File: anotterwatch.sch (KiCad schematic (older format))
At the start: 55 parts, among them J1 USB_C_Receptacle_USB2.0, J3 Micro_SD_Card, Q1 AO3400, Q3 npn, Q4 npn, U1 TP4056, U12 BMI270, U2 ESP32, U3 CH340C, U4 ST7789V

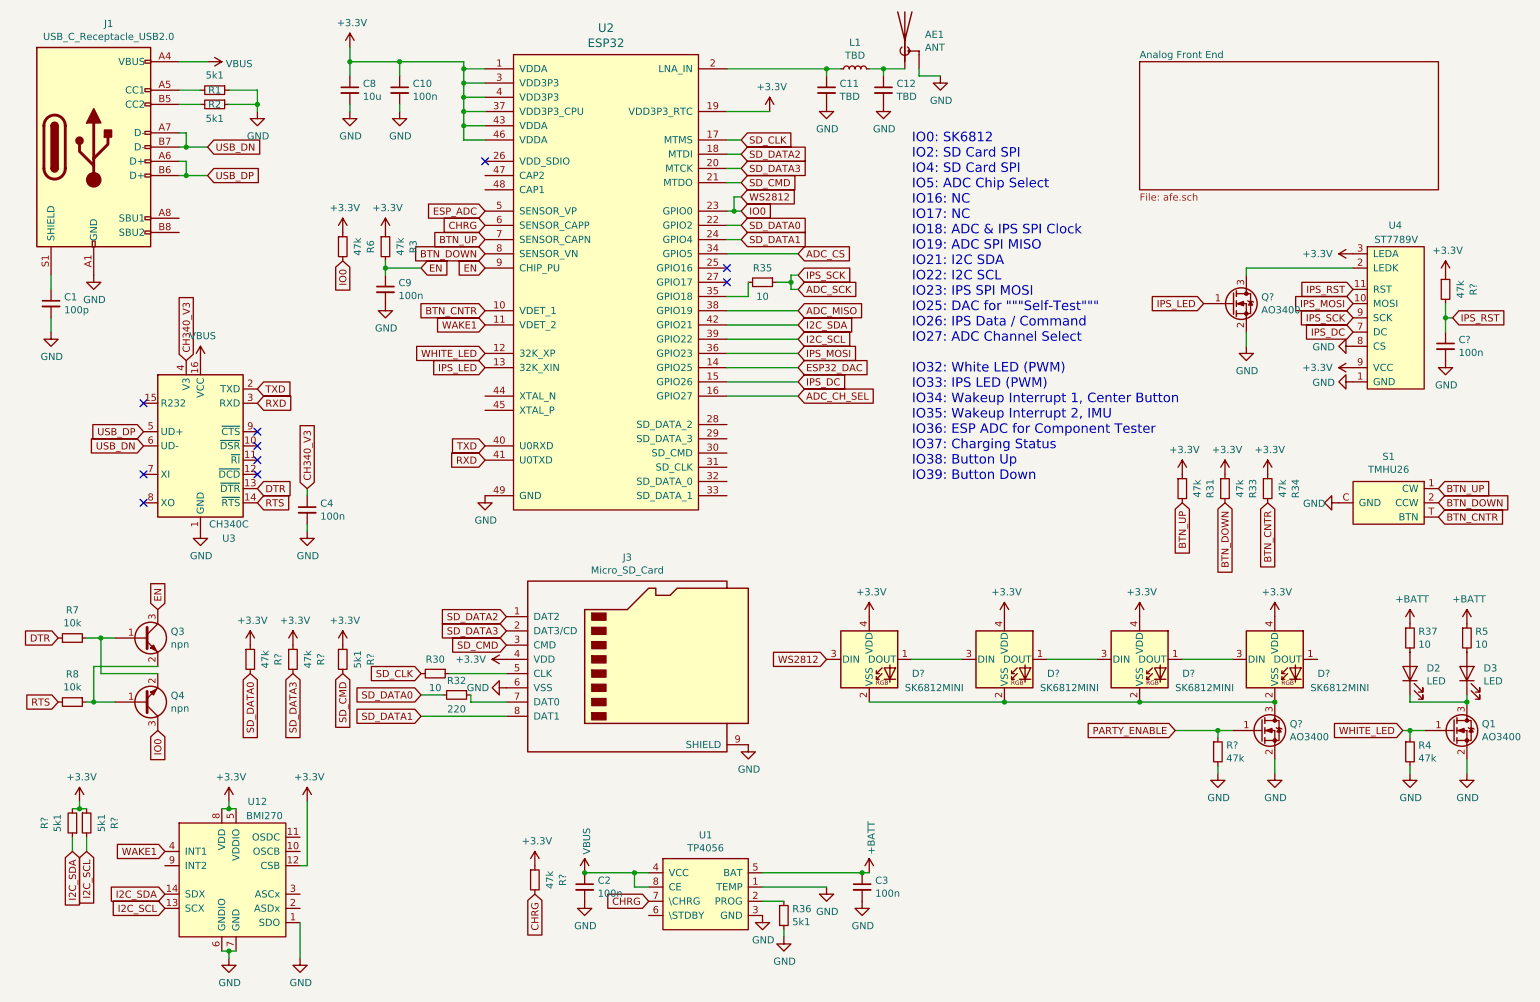
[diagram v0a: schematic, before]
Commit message: ADD: speaker
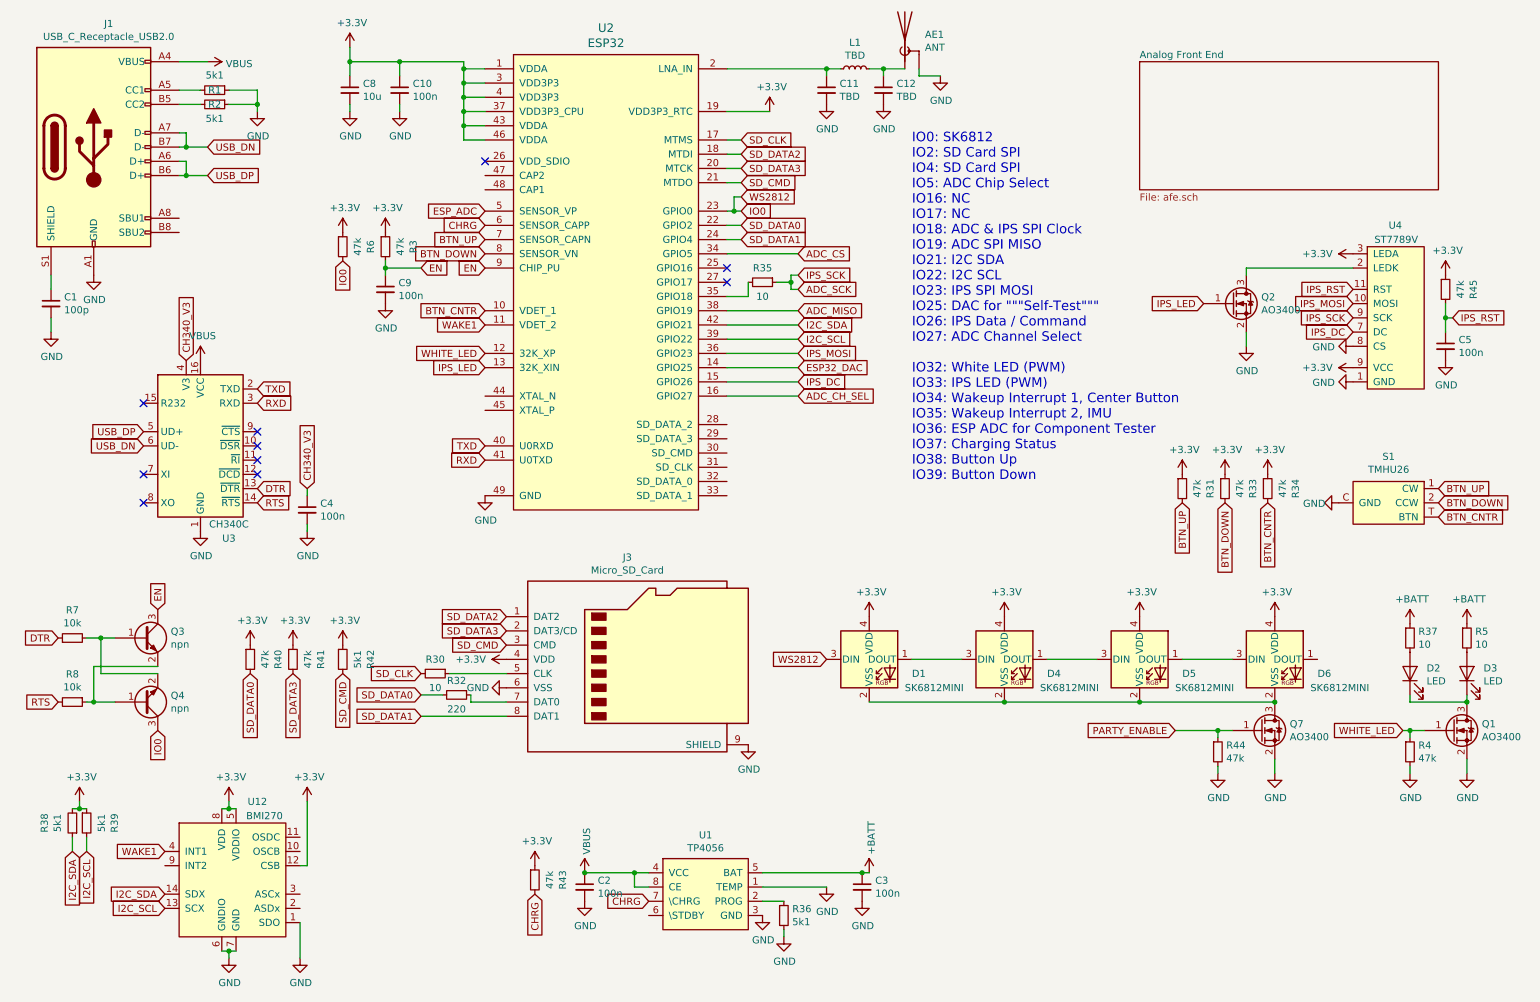
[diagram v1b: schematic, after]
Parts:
- gave numbers to parts that had none: 15
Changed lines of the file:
@@
 	9300 3100 9300 3200
 $Comp
-L power:+3.3V #PWR?
+L power:+3.3V #PWR057
 U 1 1 5C88B593
 P 10050 3350
-F 0 "#PWR?" H 10050 3200 50  0001 C CNN
+F 0 "#PWR057" H 10050 3200 50  0001 C CNN
 F 1 "+3.3V" V 10050 3600 50  0000 C CNN
 F 2 "" H 10050 3350 50  0001 C CNN
@@
 CHRG
 $Comp
-L Device:R_Small R?
+L Device:R_Small R43
 U 1 1 5C8A8B52
 P 4300 6950
-F 0 "R?" V 4496 6950 50  0000 C CNN
+F 0 "R43" V 4496 6950 50  0000 C CNN
 F 1 "47k" V 4405 6950 50  0000 C CNN
 F 2 "Resistor_SMD:R_0603_1608Metric" H 4300 6950 50  0001 C CNN
@@
 $EndComp
 $Comp
-L power:+3.3V #PWR?
+L power:+3.3V #PWR049
 U 1 1 5C8A8B59
 P 4300 6850
-F 0 "#PWR?" H 4300 6700 50  0001 C CNN
+F 0 "#PWR049" H 4300 6700 50  0001 C CNN
 F 1 "+3.3V" H 4315 7023 50  0000 C CNN
 F 2 "" H 4300 6850 50  0001 C CNN
@@
 $EndComp
 $Comp
-L Device:Q_NMOS_GSD Q?
+L Device:Q_NMOS_GSD Q2
 U 1 1 5C8ADB53
 P 9200 2900
-F 0 "Q?" H 9405 2946 50  0000 L CNN
+F 0 "Q2" H 9405 2946 50  0000 L CNN
 F 1 "AO3400" H 9405 2855 50  0000 L CNN
 F 2 "Package_TO_SOT_SMD:SOT-23" H 9400 3000 50  0001 C CNN
@@
 IPS_MOSI
 $Comp
-L power:+3.3V #PWR?
+L power:+3.3V #PWR03
 U 1 1 5C8AE78F
 P 2150 6400
-F 0 "#PWR?" H 2150 6250 50  0001 C CNN
+F 0 "#PWR03" H 2150 6250 50  0001 C CNN
 F 1 "+3.3V" H 2165 6573 50  0000 C CNN
 F 2 "" H 2150 6400 50  0001 C CNN
@@
 Connection ~ 2150 6450
 $Comp
-L power:GND #PWR?
+L power:GND #PWR06
 U 1 1 5C8B6736
 P 2150 7500
-F 0 "#PWR?" H 2150 7250 50  0001 C CNN
+F 0 "#PWR06" H 2150 7250 50  0001 C CNN
 F 1 "GND" H 2155 7327 50  0000 C CNN
 F 2 "" H 2150 7500 50  0001 C CNN
@@
 Connection ~ 2150 7450
 $Comp
-L power:GND #PWR?
+L power:GND #PWR046
 U 1 1 5C8C0040
 P 2650 7500
-F 0 "#PWR?" H 2650 7250 50  0001 C CNN
+F 0 "#PWR046" H 2650 7250 50  0001 C CNN
 F 1 "GND" H 2655 7327 50  0000 C CNN
 F 2 "" H 2650 7500 50  0001 C CNN
@@
 I2C_SCL
 $Comp
-L power:+3.3V #PWR?
+L power:+3.3V #PWR047
 U 1 1 5C8CE265
 P 2700 6400
-F 0 "#PWR?" H 2700 6250 50  0001 C CNN
+F 0 "#PWR047" H 2700 6250 50  0001 C CNN
 F 1 "+3.3V" H 2715 6573 50  0000 C CNN
 F 2 "" H 2700 6400 50  0001 C CNN
@@
 I2C_SCL
 $Comp
-L power:+3.3V #PWR?
+L power:+3.3V #PWR01
 U 1 1 5C8EA6C1
 P 1100 6400
-F 0 "#PWR?" H 1100 6250 50  0001 C CNN
+F 0 "#PWR01" H 1100 6250 50  0001 C CNN
 F 1 "+3.3V" H 1115 6573 50  0000 C CNN
 F 2 "" H 1100 6400 50  0001 C CNN
@@
 $EndComp
 $Comp
-L Device:R_Small R?
+L Device:R_Small R39
 U 1 1 5C8EA748
 P 1150 6550
-F 0 "R?" V 1346 6550 50  0000 C CNN
+F 0 "R39" V 1346 6550 50  0000 C CNN
 F 1 "5k1" V 1255 6550 50  0000 C CNN
 F 2 "Resistor_SMD:R_0603_1608Metric" H 1150 6550 50  0001 C CNN
@@
 $EndComp
 $Comp
-L Device:R_Small R?
+L Device:R_Small R38
 U 1 1 5C8EA7F2
 P 1050 6550
-F 0 "R?" V 1246 6550 50  0000 C CNN
+F 0 "R38" V 1246 6550 50  0000 C CNN
 F 1 "5k1" V 1155 6550 50  0000 C CNN
 F 2 "Resistor_SMD:R_0603_1608Metric" H 1050 6550 50  0001 C CNN
@@
 SD_CMD
 $Comp
-L Device:R_Small R?
+L Device:R_Small R40
 U 1 1 5CA0E021
 P 2300 5400
-F 0 "R?" V 2496 5400 50  0000 C CNN
+F 0 "R40" V 2496 5400 50  0000 C CNN
 F 1 "47k" V 2405 5400 50  0000 C CNN
 F 2 "Resistor_SMD:R_0603_1608Metric" H 2300 5400 50  0001 C CNN
@@
 $EndComp
 $Comp
-L Device:R_Small R?
+L Device:R_Small R41
 U 1 1 5CA0E103
 P 2600 5400
-F 0 "R?" V 2796 5400 50  0000 C CNN
+F 0 "R41" V 2796 5400 50  0000 C CNN
 F 1 "47k" V 2705 5400 50  0000 C CNN
 F 2 "Resistor_SMD:R_0603_1608Metric" H 2600 5400 50  0001 C CNN
@@
 $EndComp
 $Comp
-L power:+3.3V #PWR?
+L power:+3.3V #PWR039
 U 1 1 5CA0E26B
 P 2300 5300
-F 0 "#PWR?" H 2300 5150 50  0001 C CNN
+F 0 "#PWR039" H 2300 5150 50  0001 C CNN
 F 1 "+3.3V" H 2315 5473 50  0000 C CNN
 F 2 "" H 2300 5300 50  0001 C CNN
@@
 $EndComp
 $Comp
-L power:+3.3V #PWR?
+L power:+3.3V #PWR040
 U 1 1 5CA0E2FA
 P 2600 5300
-F 0 "#PWR?" H 2600 5150 50  0001 C CNN
+F 0 "#PWR040" H 2600 5150 50  0001 C CNN
 F 1 "+3.3V" H 2615 5473 50  0000 C CNN
 F 2 "" H 2600 5300 50  0001 C CNN
@@
 $EndComp
 $Comp
-L Device:R_Small R?
+L Device:R_Small R42
 U 1 1 5CA0E451
 P 2950 5400
-F 0 "R?" V 3146 5400 50  0000 C CNN
+F 0 "R42" V 3146 5400 50  0000 C CNN
 F 1 "5k1" V 3055 5400 50  0000 C CNN
 F 2 "Resistor_SMD:R_0603_1608Metric" H 2950 5400 50  0001 C CNN
@@
 $EndComp
 $Comp
-L power:+3.3V #PWR?
+L power:+3.3V #PWR048
 U 1 1 5CA0E551
 P 2950 5300
-F 0 "#PWR?" H 2950 5150 50  0001 C CNN
+F 0 "#PWR048" H 2950 5150 50  0001 C CNN
 F 1 "+3.3V" H 2965 5473 50  0000 C CNN
 F 2 "" H 2950 5300 50  0001 C CNN
@@
 SD_DATA1
 $Comp
-L LED:SK6812MINI D?
+L LED:SK6812MINI D1
 U 1 1 5CA5E3A4
 P 6650 5400
-F 0 "D?" H 6950 5300 50  0000 L CNN
+F 0 "D1" H 6950 5300 50  0000 L CNN
 F 1 "SK6812MINI" H 6900 5200 50  0000 L CNN
 F 2 "LED_SMD:LED_SK6812MINI_PLCC4_3.5x3.5mm_P1.75mm" H 6700 5100 50  0001 L TNN
@@
 $EndComp
 $Comp
-L LED:SK6812MINI D?
+L LED:SK6812MINI D4
 U 1 1 5CA5E80C
 P 7600 5400
-F 0 "D?" H 7900 5300 50  0000 L CNN
+F 0 "D4" H 7900 5300 50  0000 L CNN
 F 1 "SK6812MINI" H 7850 5200 50  0000 L CNN
 F 2 "LED_SMD:LED_SK6812MINI_PLCC4_3.5x3.5mm_P1.75mm" H 7650 5100 50  0001 L TNN
@@
 $EndComp
 $Comp
-L LED:SK6812MINI D?
+L LED:SK6812MINI D5
 U 1 1 5CA5E8A0
 P 8550 5400
-F 0 "D?" H 8850 5300 50  0000 L CNN
+F 0 "D5" H 8850 5300 50  0000 L CNN
 F 1 "SK6812MINI" H 8800 5200 50  0000 L CNN
 F 2 "LED_SMD:LED_SK6812MINI_PLCC4_3.5x3.5mm_P1.75mm" H 8600 5100 50  0001 L TNN
@@
 $EndComp
 $Comp
-L LED:SK6812MINI D?
+L LED:SK6812MINI D6
 U 1 1 5CA5E934
 P 9500 5400
-F 0 "D?" H 9800 5300 50  0000 L CNN
+F 0 "D6" H 9800 5300 50  0000 L CNN
 F 1 "SK6812MINI" H 9750 5200 50  0000 L CNN
 F 2 "LED_SMD:LED_SK6812MINI_PLCC4_3.5x3.5mm_P1.75mm" H 9550 5100 50  0001 L TNN
@@
 	8850 5400 9200 5400
 $Comp
-L power:+3.3V #PWR?
+L power:+3.3V #PWR050
 U 1 1 5CA6F675
 P 6650 5100
-F 0 "#PWR?" H 6650 4950 50  0001 C CNN
+F 0 "#PWR050" H 6650 4950 50  0001 C CNN
 F 1 "+3.3V" H 6665 5273 50  0000 C CNN
 F 2 "" H 6650 5100 50  0001 C CNN
@@
 $EndComp
 $Comp
-L power:+3.3V #PWR?
+L power:+3.3V #PWR051
 U 1 1 5CA6F6ED
 P 7600 5100
-F 0 "#PWR?" H 7600 4950 50  0001 C CNN
+F 0 "#PWR051" H 7600 4950 50  0001 C CNN
 F 1 "+3.3V" H 7615 5273 50  0000 C CNN
 F 2 "" H 7600 5100 50  0001 C CNN
@@
 $EndComp
 $Comp
-L power:+3.3V #PWR?
+L power:+3.3V #PWR052
 U 1 1 5CA6F75E
 P 8550 5100
-F 0 "#PWR?" H 8550 4950 50  0001 C CNN
+F 0 "#PWR052" H 8550 4950 50  0001 C CNN
 F 1 "+3.3V" H 8565 5273 50  0000 C CNN
 F 2 "" H 8550 5100 50  0001 C CNN
@@
 $EndComp
 $Comp
-L power:+3.3V #PWR?
+L power:+3.3V #PWR054
 U 1 1 5CA6F7CF
 P 9500 5100
-F 0 "#PWR?" H 9500 4950 50  0001 C CNN
+F 0 "#PWR054" H 9500 4950 50  0001 C CNN
 F 1 "+3.3V" H 9515 5273 50  0000 C CNN
 F 2 "" H 9500 5100 50  0001 C CNN
@@
 $EndComp
 $Comp
-L Device:Q_NMOS_GSD Q?
+L Device:Q_NMOS_GSD Q7
 U 1 1 5CA73CF2
 P 9400 5900
-F 0 "Q?" H 9605 5946 50  0000 L CNN
+F 0 "Q7" H 9605 5946 50  0000 L CNN
 F 1 "AO3400" H 9605 5855 50  0000 L CNN
 F 2 "Package_TO_SOT_SMD:SOT-23" H 9600 6000 50  0001 C CNN
@@
 $EndComp
 $Comp
-L power:GND #PWR?
+L power:GND #PWR055
 U 1 1 5CA73CF9
 P 9500 6200
-F 0 "#PWR?" H 9500 5950 50  0001 C CNN
+F 0 "#PWR055" H 9500 5950 50  0001 C CNN
 F 1 "GND" H 9505 6027 50  0000 C CNN
 F 2 "" H 9500 6200 50  0001 C CNN
@@
 	9500 6200 9500 6100
 $Comp
-L Device:R_Small R?
+L Device:R_Small R44
 U 1 1 5CA73D00
 P 9100 6050
-F 0 "R?" H 9159 6096 50  0000 L CNN
+F 0 "R44" H 9159 6096 50  0000 L CNN
 F 1 "47k" H 9159 6005 50  0000 L CNN
 F 2 "Resistor_SMD:R_0603_1608Metric" H 9100 6050 50  0001 C CNN
@@
 	9100 5900 9200 5900
 $Comp
-L power:GND #PWR?
+L power:GND #PWR053
 U 1 1 5CA73D0A
 P 9100 6200
-F 0 "#PWR?" H 9100 5950 50  0001 C CNN
+F 0 "#PWR053" H 9100 5950 50  0001 C CNN
 F 1 "GND" H 9105 6027 50  0000 C CNN
 F 2 "" H 9100 6200 50  0001 C CNN
@@
 Connection ~ 10450 5900
 $Comp
-L power:GND #PWR?
+L power:GND #PWR056
 U 1 1 5CB2DE24
 P 10050 3200
-F 0 "#PWR?" H 10050 2950 50  0001 C CNN
+F 0 "#PWR056" H 10050 2950 50  0001 C CNN
 F 1 "GND" V 10055 3072 50  0000 R CNN
 F 2 "" H 10050 3200 50  0001 C CNN
@@
 IPS_RST
 $Comp
-L Device:R_Small R?
+L Device:R_Small R45
 U 1 1 5CB2EA91
 P 10700 2800
-F 0 "R?" V 10896 2800 50  0000 C CNN
+F 0 "R45" V 10896 2800 50  0000 C CNN
 F 1 "47k" V 10805 2800 50  0000 C CNN
 F 2 "Resistor_SMD:R_0603_1608Metric" H 10700 2800 50  0001 C CNN
@@
 $EndComp
 $Comp
-L power:+3.3V #PWR?
+L power:+3.3V #PWR058
 U 1 1 5CB2EA98
 P 10700 2700
-F 0 "#PWR?" H 10700 2550 50  0001 C CNN
+F 0 "#PWR058" H 10700 2550 50  0001 C CNN
 F 1 "+3.3V" H 10715 2873 50  0000 C CNN
 F 2 "" H 10700 2700 50  0001 C CNN
@@
 $EndComp
 $Comp
-L Device:C_Small C?
+L Device:C_Small C5
 U 1 1 5CB333E1
 P 10700 3200
-F 0 "C?" H 10792 3246 50  0000 L CNN
+F 0 "C5" H 10792 3246 50  0000 L CNN
 F 1 "100n" H 10792 3155 50  0000 L CNN
 F 2 "Capacitor_SMD:C_0603_1608Metric" H 10700 3200 50  0001 C CNN
@@
 $EndComp
 $Comp
-L power:GND #PWR?
+L power:GND #PWR059
 U 1 1 5CB333E8
 P 10700 3300
-F 0 "#PWR?" H 10700 3050 50  0001 C CNN
+F 0 "#PWR059" H 10700 3050 50  0001 C CNN
 F 1 "GND" H 10705 3127 50  0000 C CNN
 F 2 "" H 10700 3300 50  0001 C CNN

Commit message: added power schematics
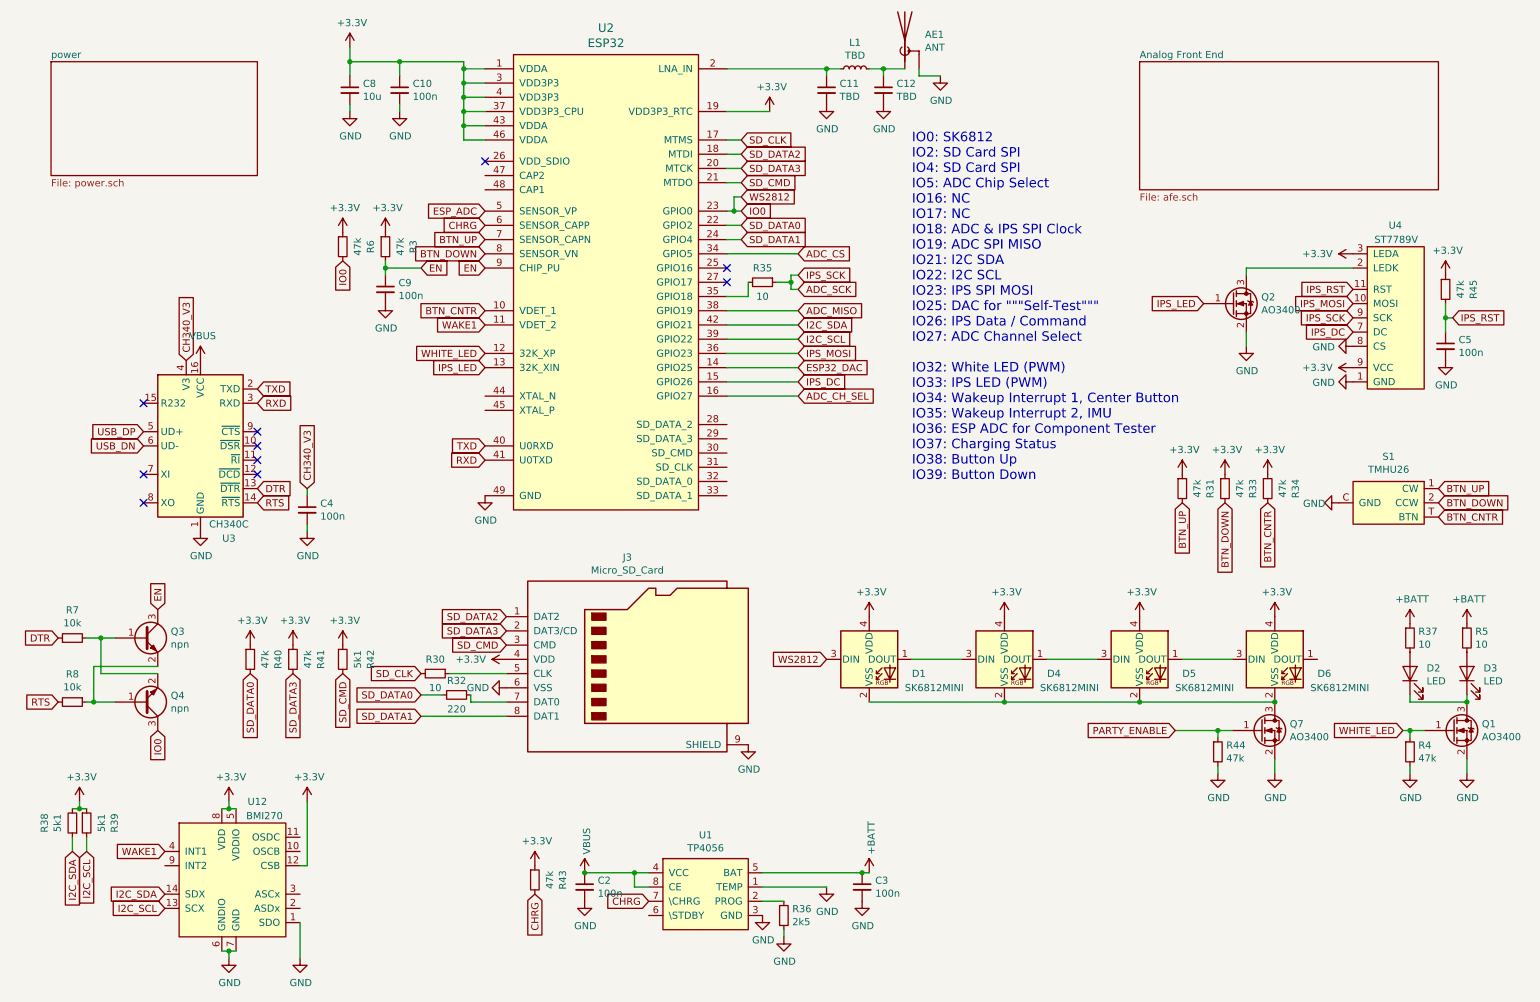
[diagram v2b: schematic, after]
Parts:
- removed C1: 100p, Capacitor_SMD:C_0603_1608Metric, symbol Device:C_Small
- removed J1: USB_C_Receptacle_USB2.0, badgelib:USB-C 16Pin, symbol anotterwatch-rescue:USB_C_Receptacle_USB2.0-Connector
- removed R1, R2: 5k1, Resistor_SMD:R_0603_1608Metric, symbol Device:R_Small
- R36: value 5k1 -> 2k5
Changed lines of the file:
@@
 $Descr A4 11693 8268
 encoding utf-8
-Sheet 1 2
+Sheet 1 3
 Title ""
 Date ""
@@
 Comment4 ""
 $EndDescr
-$Comp
-L anotterwatch-rescue:USB_C_Receptacle_USB2.0-Connector J1
-U 1 1 5C6DC086
-P 1200 1800
-F 0 "J1" H 1305 2667 50  0000 C CNN
-F 1 "USB_C_Receptacle_USB2.0" H 1305 2576 50  0000 C CNN
-F 2 "badgelib:USB-C 16Pin" H 1350 1800 50  0001 C CNN
-F 3 "https://nl.aliexpress.com/item/100PCS-LOT-USB-connector-Type-C-3-1-Female-connector-16Pin-SMD-SMT-Type-with-4/32822609480.html" H 1350 1800 50  0001 C CNN
-	1    1200 1800
-	1    0    0    -1
-$EndComp
-$Comp
-L power:GND #PWR0101
-U 1 1 5C6E198C
-P 1200 2700
-F 0 "#PWR0101" H 1200 2450 50  0001 C CNN
-F 1 "GND" H 1205 2527 50  0000 C CNN
-F 2 "" H 1200 2700 50  0001 C CNN
-F 3 "" H 1200 2700 50  0001 C CNN
-	1    1200 2700
-	1    0    0    -1
-$EndComp
-$Comp
-L power:GND #PWR0102
-U 1 1 5C6E19B1
-P 900 3100
-F 0 "#PWR0102" H 900 2850 50  0001 C CNN
-F 1 "GND" H 905 2927 50  0000 C CNN
-F 2 "" H 900 3100 50  0001 C CNN
-F 3 "" H 900 3100 50  0001 C CNN
-	1    900  3100
-	1    0    0    -1
-$EndComp
-$Comp
-L Device:C_Small C1
-U 1 1 5C6E19F9
-P 900 2900
-F 0 "C1" H 992 2946 50  0000 L CNN
-F 1 "100p" H 992 2855 50  0000 L CNN
-F 2 "Capacitor_SMD:C_0603_1608Metric" H 900 2900 50  0001 C CNN
-F 3 "~" H 900 2900 50  0001 C CNN
-	1    900  2900
-	1    0    0    -1
-$EndComp
-Wire Wire Line
-	900  3100 900  3000
-Wire Wire Line
-	900  2800 900  2700
-$Comp
-L Device:R_Small R1
-U 1 1 5C6E1AEB
-P 2050 1400
-F 0 "R1" V 2050 1400 50  0000 C CNN
-F 1 "5k1" V 1945 1400 50  0000 C CNN
-F 2 "Resistor_SMD:R_0603_1608Metric" H 2050 1400 50  0001 C CNN
-F 3 "~" H 2050 1400 50  0001 C CNN
-	1    2050 1400
-	0    1    1    0
-$EndComp
-$Comp
-L Device:R_Small R2
-U 1 1 5C6E1B28
-P 2050 1500
-F 0 "R2" V 2050 1500 50  0000 C CNN
-F 1 "5k1" V 2150 1500 50  0000 C CNN
-F 2 "Resistor_SMD:R_0603_1608Metric" H 2050 1500 50  0001 C CNN
-F 3 "~" H 2050 1500 50  0001 C CNN
-	1    2050 1500
-	0    1    1    0
-$EndComp
-Wire Wire Line
-	1950 1400 1800 1400
-Wire Wire Line
-	1800 1500 1950 1500
-Wire Wire Line
-	2150 1500 2350 1500
-Wire Wire Line
-	2350 1400 2150 1400
-Wire Wire Line
-	2350 1400 2350 1500
-Connection ~ 2350 1500
-Wire Wire Line
-	2350 1500 2350 1550
-$Comp
-L power:GND #PWR0103
-U 1 1 5C6E1C3F
-P 2350 1550
-F 0 "#PWR0103" H 2350 1300 50  0001 C CNN
-F 1 "GND" H 2355 1377 50  0000 C CNN
-F 2 "" H 2350 1550 50  0001 C CNN
-F 3 "" H 2350 1550 50  0001 C CNN
-	1    2350 1550
-	1    0    0    -1
-$EndComp
-$Comp
-L power:VBUS #PWR0104
-U 1 1 5C6E1CAC
-P 2000 1200
-F 0 "#PWR0104" H 2000 1050 50  0001 C CNN
-F 1 "VBUS" V 2015 1328 50  0000 L CNN
-F 2 "" H 2000 1200 50  0001 C CNN
-F 3 "" H 2000 1200 50  0001 C CNN
-	1    2000 1200
-	0    1    1    0
-$EndComp
-Wire Wire Line
-	2000 1200 1800 1200
-Wire Wire Line
-	1800 1700 1850 1700
-Wire Wire Line
-	1850 1700 1850 1800
-Wire Wire Line
-	1800 1800 1850 1800
-Connection ~ 1850 1800
-Wire Wire Line
-	1800 2000 1850 2000
-Wire Wire Line
-	1850 2000 1850 1900
-Wire Wire Line
-	1850 1900 1800 1900
-Connection ~ 1850 2000
-Wire Wire Line
-	1850 1800 2000 1800
-Wire Wire Line
-	1850 2000 2000 2000
 $Comp
 L Device:LED D3
@@
 	1    0    0    -1
 $EndComp
-Text GLabel 2000 1800 2    50   Input ~ 0
-USB_DN
-Text GLabel 2000 2000 2    50   Input ~ 0
-USB_DP
 $Comp
 L power:GND #PWR0118
@@
 P 6050 7200
 F 0 "R36" H 6109 7246 50  0000 L CNN
-F 1 "5k1" H 6109 7155 50  0000 L CNN
+F 1 "2k5" H 6109 7155 50  0000 L CNN
 F 2 "Resistor_SMD:R_0603_1608Metric" H 6050 7200 50  0001 C CNN
 F 3 "~" H 6050 7200 50  0001 C CNN
@@
 Wire Wire Line
 	10700 3000 10700 2900
+$Sheet
+S 900  1200 1450 800
+U 5C753B69
+F0 "power" 50
+F1 "power.sch" 50
+$EndSheet
 $EndSCHEMATC
